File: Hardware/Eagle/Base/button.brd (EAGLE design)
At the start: 29.9 x 45.8 mm, 11 parts, among them SW2 SPST_TACT-EVQQ2, X1 1365-10

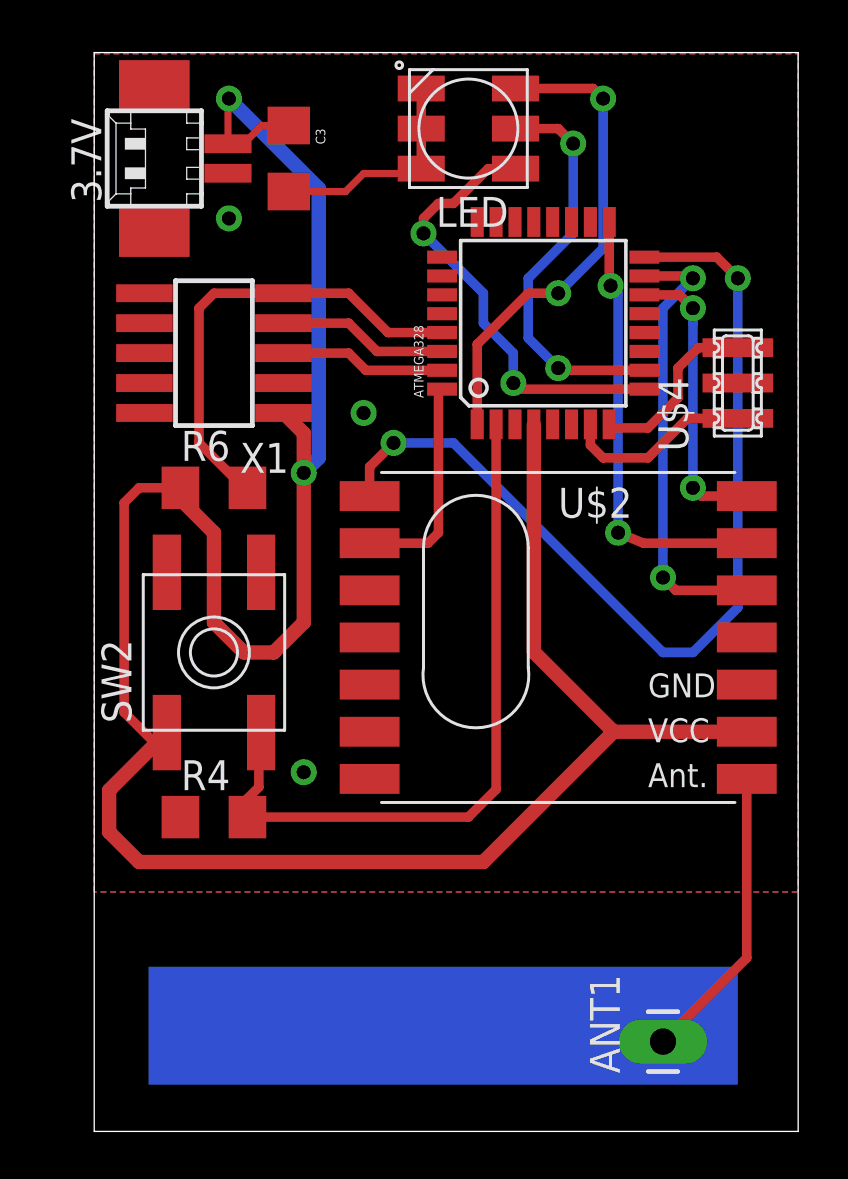
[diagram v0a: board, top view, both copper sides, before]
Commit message: Button hardware changes
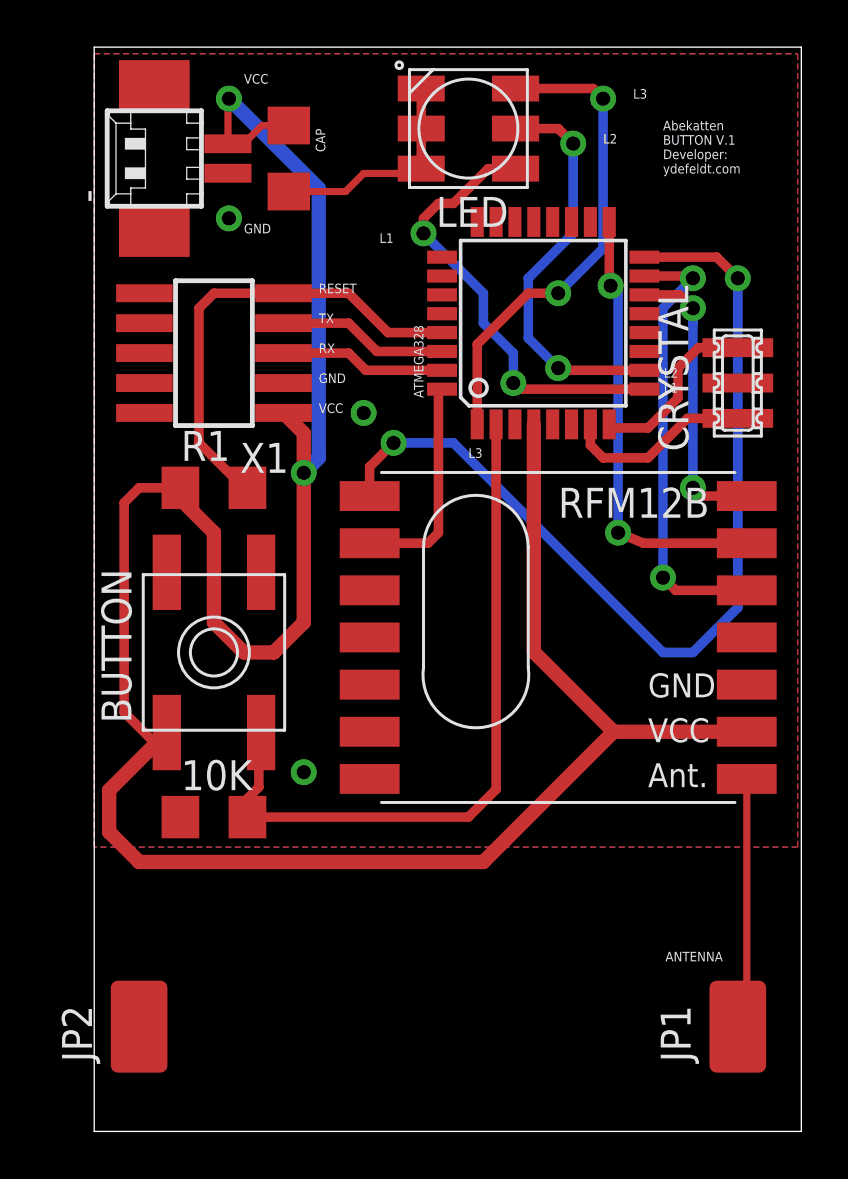
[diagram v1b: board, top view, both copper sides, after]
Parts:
- removed ANT1: M01PTH_LONGPAD, SparkFun:1X01_LONGPAD
- added JP1, JP2: M01SMD, SparkFun:LUXEON-PAD
- CRYSTAL: value (none) -> 23
- R1: value 10k -> 10K
- RFM12B: value RFM12BRMF12BGND -> RFM12B
- renumbered 3.7V to -, C3 to CAP, R4 to 10K, R6 to R1, SW2 to BUTTON, U$2 to RFM12B, U$4 to CRYSTAL
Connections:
- net N$25: now also JP1.P$1; no longer ANT1.1
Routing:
- net N$25: track 12.6 -> 10.9 mm
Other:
- board size 29.9 x 45.8 mm -> 30 x 46 mm
- board text added: "ANTENNA"
- board text added: "Abekatten BUTTON V.1 Developer: ydefeldt.com"
- board text added: "GND"
- board text added: "L1"
- board text added: "L2"
- board text added: "L3"
- board text added: "RESET"
- board text added: "RX"
- board text added: "TX"
- board text added: "VCC"
